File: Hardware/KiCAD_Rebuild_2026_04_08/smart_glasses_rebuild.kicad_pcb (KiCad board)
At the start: 2 copper layers, 0 parts

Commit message: kicad manual checkpoint
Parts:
- added LS1: Small Speaker, Connector_PinHeader_2.54mm:PinHeader_1x02_P2.54mm_Vertical, F.Cu at (61.6, 60.1)
- added LS2: Small Speaker, Connector_PinHeader_2.54mm:PinHeader_1x02_P2.54mm_Vertical, F.Cu at (61.6, 66.0)
- added S1: TP4056_BMS, Connector_PinHeader_2.54mm:PinHeader_1x06_P2.54mm_Vertical, F.Cu at (72.7, 69.2)
- added U1: HW-104, Connector_PinHeader_2.54mm:PinHeader_1x09_P2.54mm_Vertical, F.Cu at (88.0, 26.1)
- added U2: MPU-6050_Breakout, Connector_PinHeader_2.54mm:PinHeader_1x08_P2.54mm_Vertical, F.Cu at (122.7, 26.0)
- added U3: INMP441, Connector_PinHeader_2.54mm:PinHeader_1x06_P2.54mm_Vertical, F.Cu at (73.0, 61.0)
- added U4: IIC_OLED, Connector_PinHeader_2.54mm:PinHeader_1x04_P2.54mm_Vertical, F.Cu at (177.4, 49.1)
- added U5: HW-763, Connector_PinHeader_2.54mm:PinHeader_1x03_P2.54mm_Vertical, F.Cu at (116.6, 44.3)
- added U7: ESP32-WROVER-dev, RebuildLib:ESP32_WROVER_DEV_2x19_WIDE, F.Cu at (141.9, 50.3)
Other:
- board outline added: 150 x 50 mm

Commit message: kicad almost done
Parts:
- moved U3 104.0 mm to (177.0, 65.1), turned to 0 degrees
- moved U5 61.9 mm to (178.3, 48.8)
- moved U2 55.0 mm to (89.6, 69.9)
- moved LS2 37.5 mm to (66.1, 28.8)
- moved U4 22.8 mm to (177.1, 26.3)
- moved LS1 18.4 mm to (79.4, 55.3), turned to -90 degrees
- moved S1 15.6 mm to (69.0, 54.1), turned to 180 degrees
- moved U1 11.2 mm to (76.9, 26.8), turned to 0 degrees
- moved U7 4.18 mm to (137.7, 49.6)
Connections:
- U1 pad 1: Net-(U1-VCC) -> Net-(U1-GND)
- U1 pad 2: Net-(U1-GND) -> Net-(U1-VCC)
- U1 pad 3: Net-(U1-LIN) -> Net-(U1-RIN)
- U1 pad 4: Net-(U1-RIN) -> Net-(U1-GND)
- U1 pad 5: Net-(U1-GND) -> Net-(U1-LIN)
- U3 pad 1: Net-(U1-VCC) -> Net-(U1-GND)
- U3 pad 2: Net-(U1-GND) -> Net-(U1-VCC)
- U3 pad 3: Net-(U3-SCK) -> Net-(U3-SD)
- U3 pad 4: Net-(U3-WS) -> Net-(U3-SCK)
- U3 pad 5: Net-(U3-SD) -> Net-(U3-WS)
- U4 pad 1: Net-(U1-VCC) -> Net-(U1-GND)
- U4 pad 2: Net-(U1-GND) -> Net-(U1-VCC)
- U5 pad 1: Net-(U1-VCC) -> Net-(U1-GND)
- U5 pad 2: Net-(U1-GND) -> Net-(U5-SIG)
- U5 pad 3: Net-(U5-SIG) -> (no net)

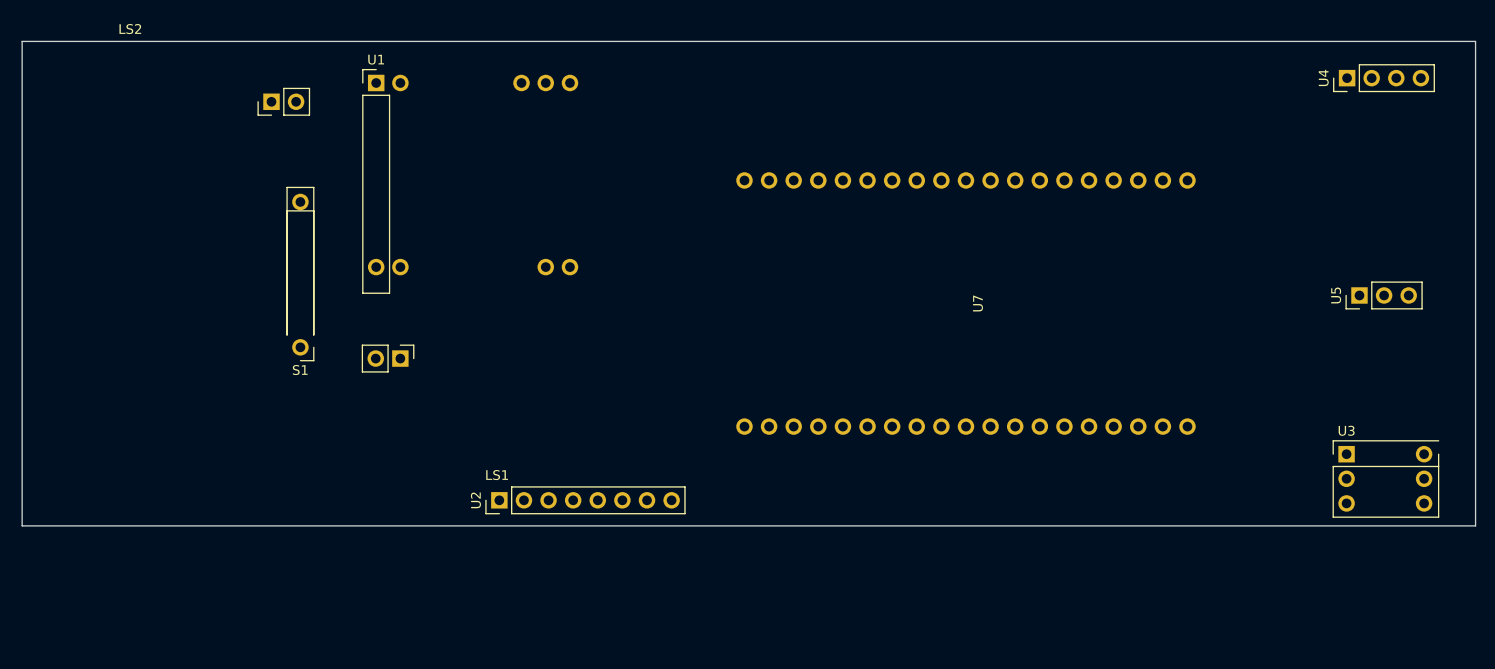
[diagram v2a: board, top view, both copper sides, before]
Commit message: kicad adding button for pwr
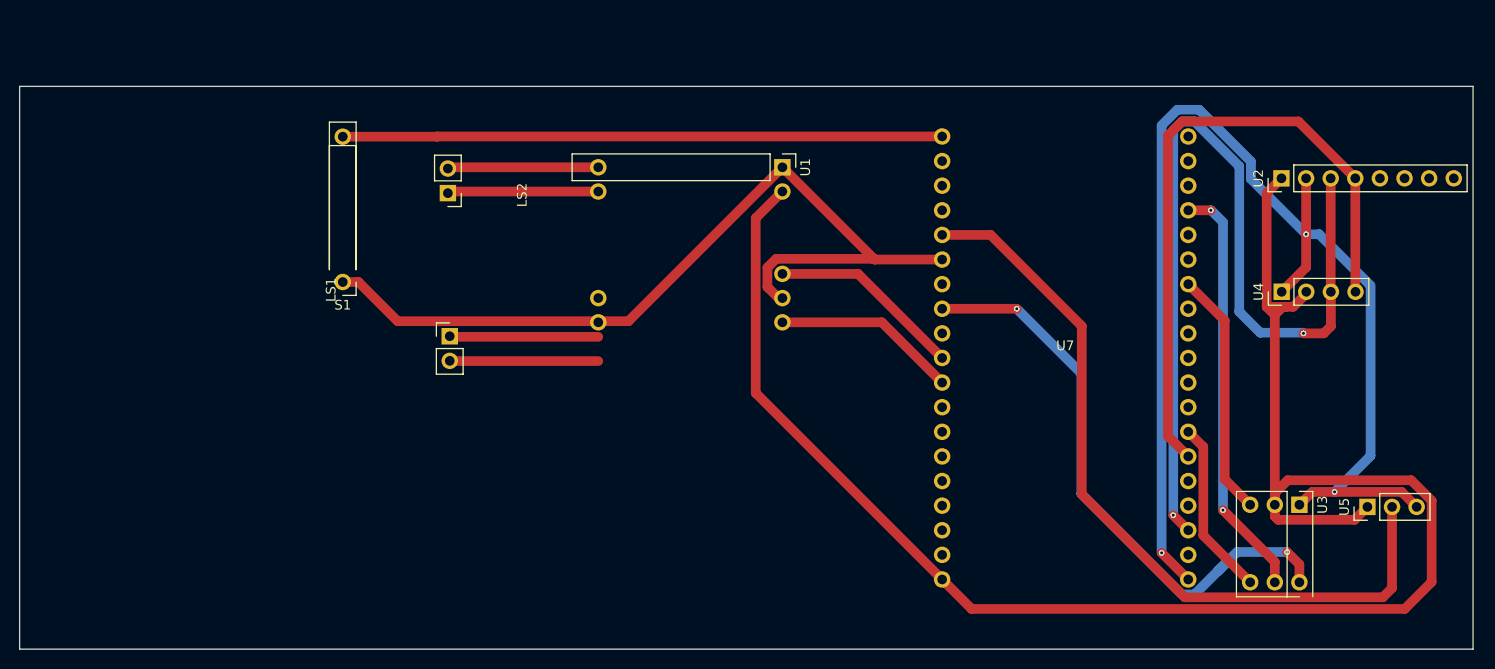
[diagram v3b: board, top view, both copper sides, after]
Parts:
- moved U2 87.3 mm to (170.3, 36.7)
- moved U1 42.8 mm to (118.8, 35.5), turned to -90 degrees
- moved LS2 30.4 mm to (84.5, 53.0), turned to 0 degrees
- moved U4 23.1 mm to (170.3, 48.4)
- moved U5 21.8 mm to (179.2, 70.6)
- moved LS1 17.8 mm to (84.3, 38.2), turned to 180 degrees
- moved U7 11.7 mm to (148.0, 55.2), turned to 0 degrees
- moved S1 8.03 mm to (73.4, 47.4)
- moved U3 7.14 mm to (172.1, 70.4), turned to -90 degrees
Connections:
- U1 pad 1: Net-(U1-GND) -> Net-(S1-OUT-)
- U1 pad 4: Net-(U1-GND) -> Net-(S1-OUT-)
- U2 pad 2: Net-(U1-GND) -> Net-(U2-GND)
- U3 pad 1: Net-(U1-GND) -> Net-(U2-GND)
- U4 pad 1: Net-(U1-GND) -> Net-(U2-GND)
- U5 pad 1: Net-(U1-GND) -> Net-(U1-VCC)
- U5 pad 3: (no net) -> Net-(U2-GND)
- U7 pad 20: Net-(U1-GND) -> Net-(U2-GND)
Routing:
- net Net-(U1-VCC): track 0.00 -> 181.7 mm
- net Net-(U2-GND): track 0.00 -> 127.7 mm, vias 0 -> 3
- net Net-(U2-SCL): track 0.00 -> 92.0 mm, vias 0 -> 2
- net Net-(S1-OUT-): track 0.00 -> 89.6 mm
- net Net-(U5-SIG): track 0.00 -> 80.9 mm
- net Net-(U2-SDA): track 0.00 -> 68.1 mm
- net Net-(U3-SCK): track 0.00 -> 62.6 mm, vias 0 -> 2
- net Net-(S1-OUT+): track 0.00 -> 61.9 mm
- net Net-(U3-WS): track 0.00 -> 43.5 mm, vias 0 -> 2
- net Net-(U3-SD): track 0.00 -> 25.4 mm
- net Net-(U1-RIN): track 0.00 -> 20.1 mm
- net Net-(U1-LIN): track 0.00 -> 19.1 mm
- net Net-(U3-L/R): track 0.00 -> 18.2 mm
- net Net-(LS1-+): track 0.00 -> 15.6 mm
- net Net-(LS1--): track 0.00 -> 15.6 mm
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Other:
- board size 150 x 50 mm -> 150 x 58.1 mm

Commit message: Kicap Prototype 2 done
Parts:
- added SW1: PWR_SW_LATCH, RebuildLib:Power_Switch_Latching_SPST_2Pin, F.Cu at (100.4, 30.4)
- moved LS2 3.95 mm to (84.5, 49.0)
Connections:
- S1 pad 6: Net-(S1-OUT-) -> GND
- U1 pad 1: Net-(S1-OUT-) -> GND
- U1 pad 4: Net-(S1-OUT-) -> GND
- U2 pad 2: Net-(U2-GND) -> GND
- U3 pad 1: Net-(U2-GND) -> GND
- U3 pad 6: Net-(U3-L/R) -> GND
- U4 pad 1: Net-(U2-GND) -> GND
- U5 pad 3: Net-(U2-GND) -> GND
- U7 pad 14: Net-(S1-OUT-) -> GND
- U7 pad 19: Net-(S1-OUT+) -> Net-(U7-5V)
- U7 pad 20: Net-(U2-GND) -> GND
- U7 pad 26: Net-(U3-L/R) -> GND
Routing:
- net GND: track 0.00 -> 309.1 mm, vias 0 -> 5
- net Net-(U2-GND): track 127.7 -> 0.00 mm, vias 3 -> 0
- net Net-(S1-OUT-): track 89.6 -> 0.00 mm
- net Net-(S1-OUT+): track 61.9 -> 27.8 mm
- net Net-(U7-5V): track 0.00 -> 29.7 mm
- net Net-(U3-L/R): track 18.2 -> 0.00 mm
- net Net-(U3-SCK): track 62.6 -> 80.7 mm
- net Net-(U1-VCC): track 181.7 -> 192.6 mm
- net Net-(U2-SCL): track 92.0 -> 94.3 mm
- net Net-(U5-SIG): track 80.9 -> 83.0 mm
- net Net-(U2-SDA): track 68.1 -> 69.7 mm
- added copper zone on B.Cu, net GND
- added copper zone on F.Cu, net GND

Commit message: Checkpoint. dont remember if broken plus added bus system pretest
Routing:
- net Net-(U2-SCL): track 94.3 -> 113.8 mm, vias 2 -> 3
- net GND: track 309.1 -> 313.5 mm
- net Net-(U1-VCC): track 192.6 -> 193.2 mm
